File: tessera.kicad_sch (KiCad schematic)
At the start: 0 parts

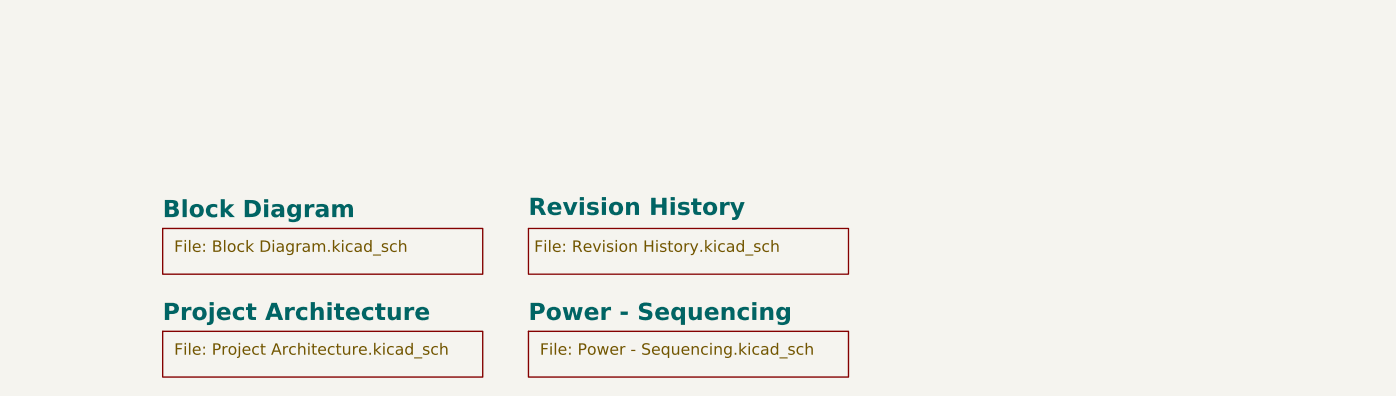
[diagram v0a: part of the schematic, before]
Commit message: feat(sch): preliminary Tessera Badge schematic
- Add sheets for LEDs, USB connector, MCU, NFC, power and STSAFE-A120.
- Drop the old placeholder sections.
- Bump the lib submodule and add IPN as a BOM column in the kibot
  outputs to reflect the DB-library parts now placed in the schematic.
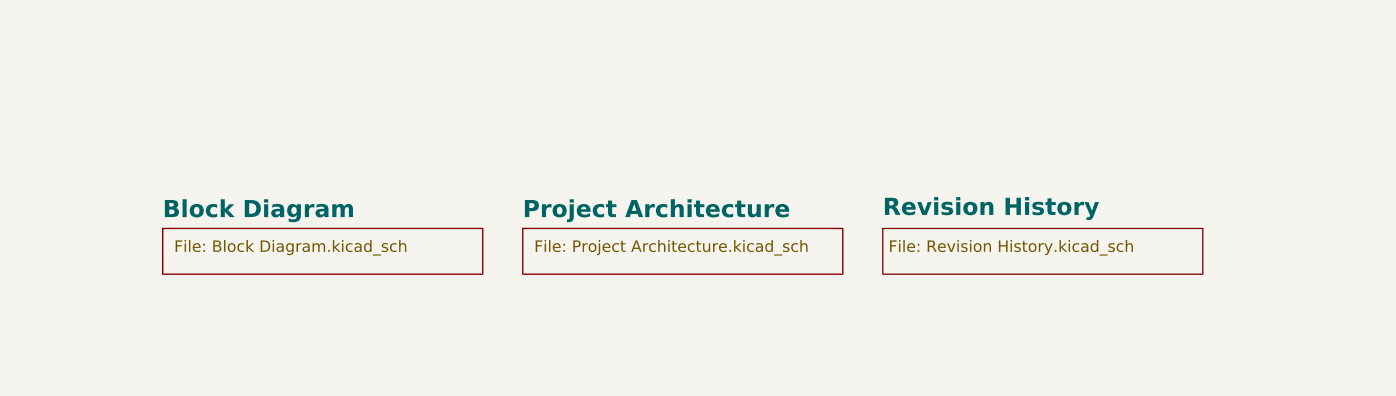
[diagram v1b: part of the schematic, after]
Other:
- removed sheet Power - Sequencing
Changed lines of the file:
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@@
 	(paper "A3")
 	(title_block
-		(date "2025-01-12")
+		(date "2026-09-08")
 		(rev "${REVISION}")
 		(company "${COMPANY}")
+	)
+	(bus_alias ""
+		(members)
 	)
 	(polyline
@@
 				(thickness 0.6)
 				(bold yes)
-				(color 140 140 140 1)
+				(color 0 0 0 1)
 			)
 			(justify left bottom)
@@
 	)
 	(sheet
-		(at 340.36 313.69)
+		(at 379.73 302.26)
 		(size 35.56 5.08)
 		(stroke
-			(width 0.1524)
+			(width 0)
 			(type solid)
 		)
@@
 			(color 0 0 0 0.0000)
 		)
-		(property "Sheetname" "Power - Sequencing"
-			(at 340.36 312.6609 0)
+		(property "Sheetname" "Revision History"
+			(at 379.73 300.99 0)
 			(effects
 				(font
@@
 			)
 		)
-		(property "Sheetfile" "Power - Sequencing.kicad_sch"
-			(at 341.63 314.96 0)
+		(property "Sheetfile" "Revision History.kicad_sch"
+			(at 380.365 303.53 0)
 			(effects
 				(font
@@
 			(project "tessera"
 				(path "/f9e05184-c88b-4a88-ae9c-ab2bdb32be7c"
-					(page "6")
-				)
-			)
-		)
-	)
-	(sheet
-		(at 340.36 302.26)
-		(size 35.56 5.08)
-		(stroke
-			(width 0)
-			(type solid)
-		)
-		(fill
-			(color 0 0 0 0.0000)
-		)
-		(property "Sheetname" "Revision History"
-			(at 340.36 300.99 0)
-			(effects
-				(font
-					(face "Times New Roman")
-					(size 1.905 1.905)
-					(bold yes)
-					(color 0 0 0 1)
-				)
-				(justify left bottom)
-			)
-		)
-		(property "Sheetfile" "Revision History.kicad_sch"
-			(at 340.995 303.53 0)
-			(effects
-				(font
-					(face "Arial")
-					(size 1.27 1.27)
-				)
-				(justify left top)
-			)
-		)
-		(instances
-			(project "tessera"
-				(path "/f9e05184-c88b-4a88-ae9c-ab2bdb32be7c"
-					(page "7")
+					(page "10")
 				)
 			)
@@
 	)
 	(sheet
-		(at 299.72 313.69)
+		(at 339.725 302.26)
 		(size 35.56 5.08)
 		(stroke
@@
 		)
 		(property "Sheetname" "Project Architecture"
-			(at 299.72 312.6609 0)
+			(at 339.725 301.2309 0)
 			(effects
 				(font
@@
 		)
 		(property "Sheetfile" "Project Architecture.kicad_sch"
-			(at 300.99 314.96 0)
+			(at 340.995 303.53 0)
 			(effects
 				(font

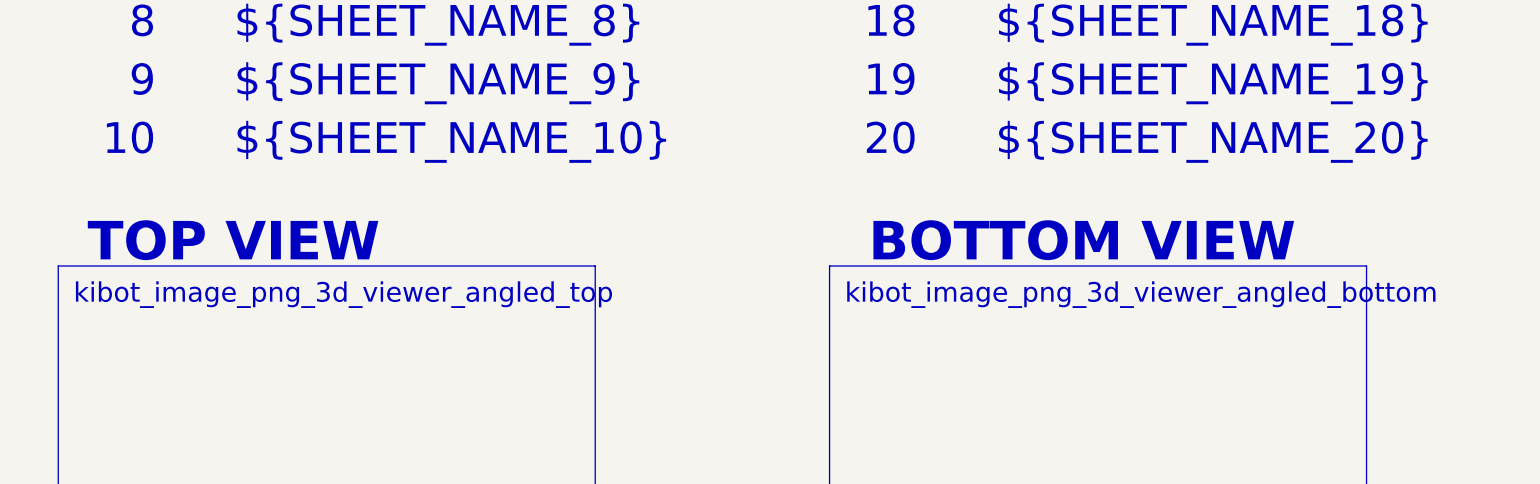
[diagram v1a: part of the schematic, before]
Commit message: fix(hardware): replace jumper/passive footprints with 0402 and refine schematics
- Replace 0-ohm jumper resistors with 0402 package equivalents
- Reduce package size on several capacitors
- Correct and simplify several schematic symbols (replaced with
  simplified equivalents where the original was overcomplicated)
- Bump lib submodule to the updated component library (renamed
  switch footprints, new Conn_01x02_MountingPin symbol, pad/pin
  numbering fixes, approved IPN assignments, Workart artwork library)
- Register Workart.pretty in fp-lib-table
- Mark J3 as DNP in mcu.kicad_sch
- Continue schematic wiring/placement (Leds.kicad_sch, tessera.kicad_sch)
  and PCB routing/placement (tessera.kicad_pcb)
- Add board outline source (Images/pcb_size.dxf, pcb_shape.FCStd) and
  silkscreen artwork sources (Logos/) for the Workart footprints
- Complete preliminary version of PCB
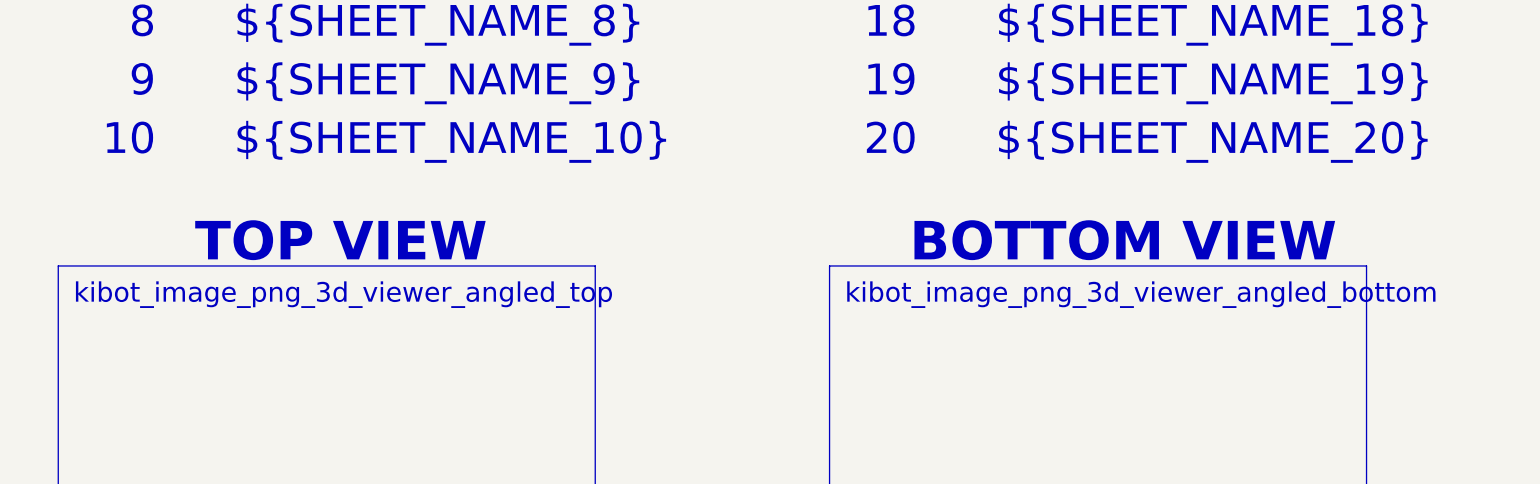
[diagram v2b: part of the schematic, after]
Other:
- title: (none) -> Front Page
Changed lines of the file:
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@@
 	(paper "A3")
 	(title_block
+		(title "Front Page")
 		(date "2026-09-08")
 		(rev "${REVISION}")
@@
 	(text "BOTTOM VIEW"
 		(exclude_from_sim no)
-		(at 128.27 166.37 0)
+		(at 133.604 166.37 0)
 		(effects
 			(font
@@
 	(text "TOP VIEW"
 		(exclude_from_sim no)
-		(at 26.67 166.37 0)
-		(effects
-			(font
+		(at 40.64 166.37 0)
+		(effects
+			(font

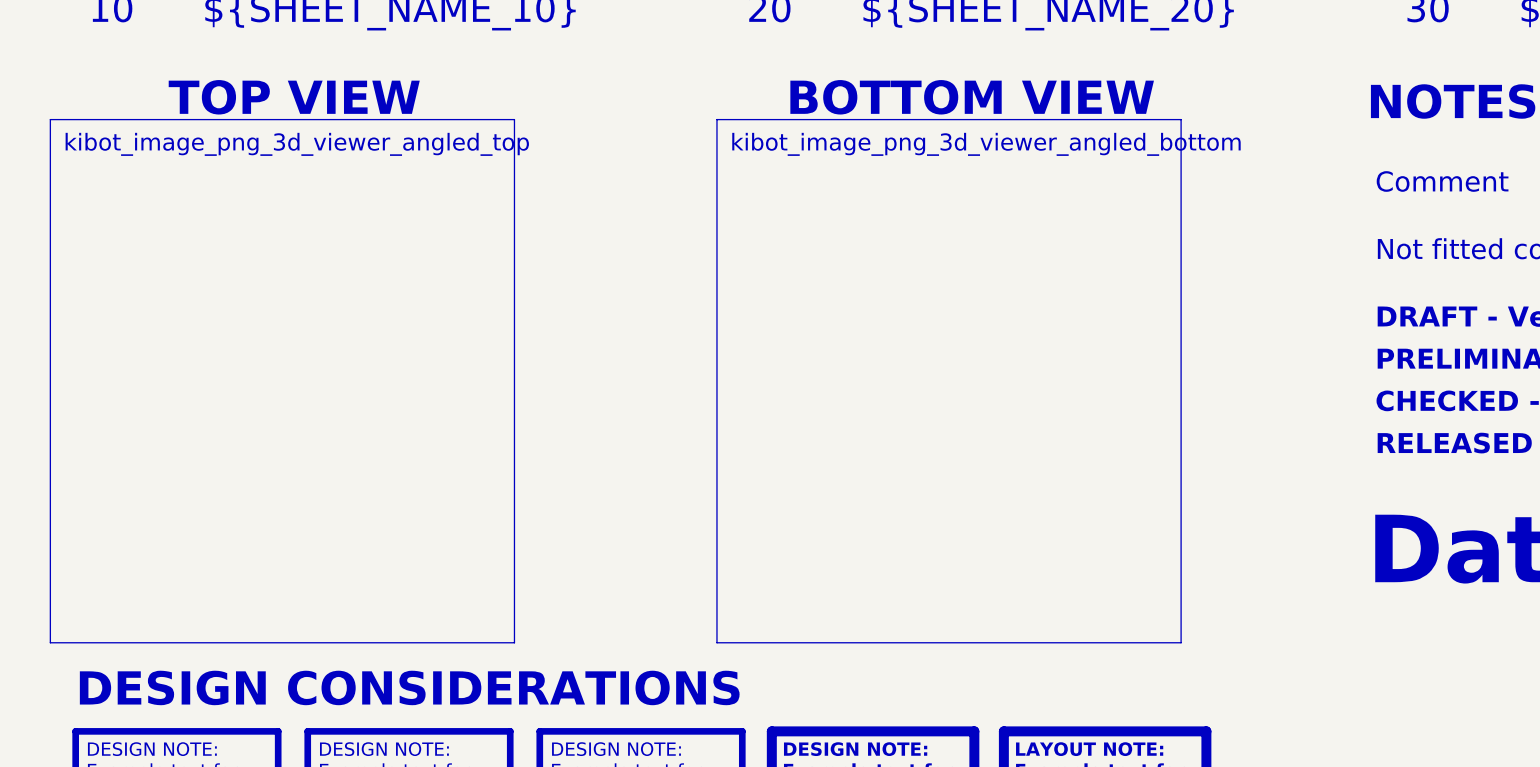
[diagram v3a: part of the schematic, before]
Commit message: fix(hardware): tighten PCB edge clearance and diff-pair rules, update logo
- Bump lib submodule: assign IPNs to another batch of approved
  capacitor selections
- Update the embedded logo artwork on every schematic sheet to the
  new Logos/logo.png
- Increase min_copper_edge_clearance to 0.5mm and raise net class
  clearance/spacing to match
- Replace the generic outer/inner-layer trace width & spacing rules
  with a dedicated "USB Diff Pair clearance to other nets" rule
  (0.2023mm, excluding intra-pair spacing already governed by the
  netclass diff_pair_gap)
- Add DRC exclusions for pre-existing clearance/copper-edge/solder-
  mask-bridge items surfaced by the tightened edge-clearance rule
- Continue schematic placement and PCB routing/placement
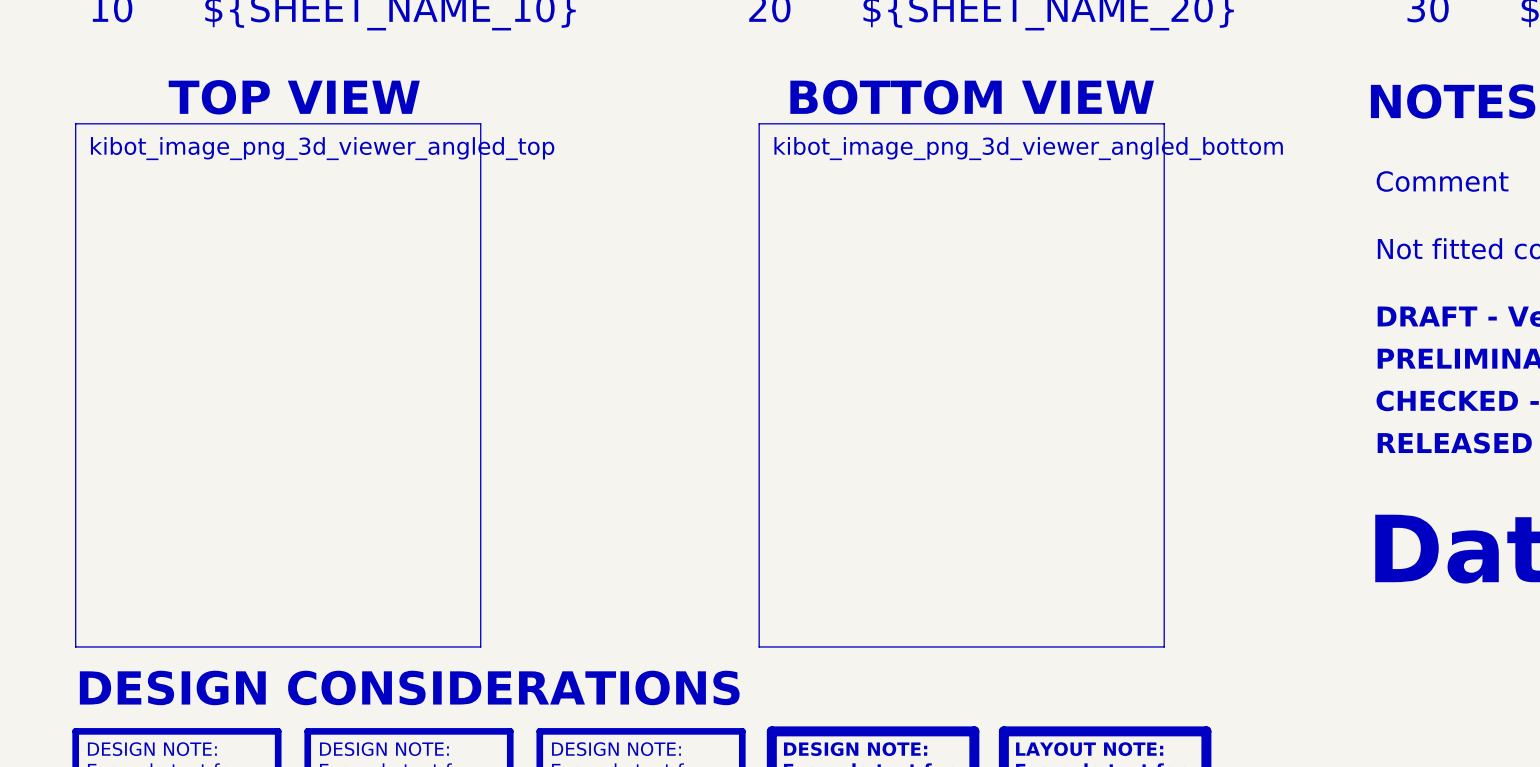
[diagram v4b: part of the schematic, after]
